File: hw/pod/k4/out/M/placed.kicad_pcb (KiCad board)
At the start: 6 copper layers, 15.5 x 12 mm, 37 parts, among them J10 TestPoint_Pad_D1.0mm, J11 TestPoint_Pad_D1.0mm, J20 CONN-SMD_BM28B0.6-30DS-2-0.35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, J3 TestPoint_Pad_D1.0mm, J4 WirePad_1.0x2.0mm, J5 TestPoint_Pad_D1.0mm, J7 TestPoint_Pad_D1.0mm, J8 TestPoint_Pad_D1.0mm, J9 TestPoint_Pad_D1.0mm, SW1 SW-SMD_4P-L3.0-W2.6-P1.85-LS3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, U2 Knowles_LGA-5_3.5x2.65mm, U3 DSBGA-8_L1.6-W0.9-R2-C4-P0.40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, U4 X2SON-4_L1.0-W1.0-P0.65-TL-EP, U6 SOT-553-5_L1.6-W1.2-P0.50-LS1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

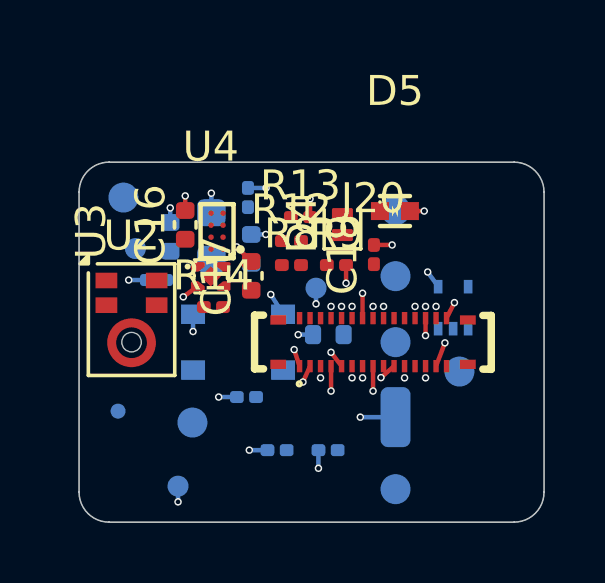
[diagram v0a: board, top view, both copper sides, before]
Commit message: K4 mic-supply filter: R30 33R + C13 on M (MIC_VDDF), k4_noise corrected (P mirror/flip, gap 0.6, JLC 6L stack K4-STACK6): worst-PSRR corner 8.0 dB unfiltered -> 26.4 dB filtered
M re-placed/re-routed (place PASS, 0 unconnected, 0 DRC errors, ERC 0 errors both); P untouched. ECR-0020 rev 5, V9, backlog, vcrm pins, plm 0/0.

Co-Authored-By: Claude Opus 5.5 <noreply@anthropic.com>
Claude-Session: https://claude.ai/code/session_01Wg997D6KFs8bxoAH56jZZJ
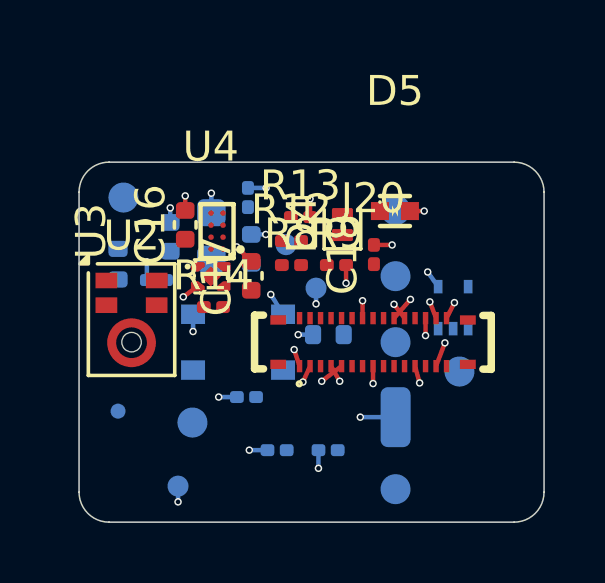
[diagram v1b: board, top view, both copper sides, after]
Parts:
- added R30: R_0402_1005Metric, R_0402_1005Metric, B.Cu at (1.30, 3.40)
- moved TP6 5.02 mm to (6.90, 2.75)
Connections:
- C13 pad 1: MIC_VDD -> MIC_VDDF
- U2 pad 5: MIC_VDD -> MIC_VDDF
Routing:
- net GND: track 16.0 -> 16.9 mm, vias 25 -> 27
- net +3V0: track 4.16 -> 4.74 mm, vias 10 -> 8
- net VBUS_SENSE: vias 1 -> 0
- net USB_DP: vias 1 -> 0
- net USB_DM: vias 1 -> 0
- net TS: vias 1 -> 0
- net MIC_VDD: vias 1 -> 0
- net MIC_DATA: vias 1 -> 0
- net MIC_CLK: vias 1 -> 0
- net I2C_SDA: vias 1 -> 0
- net I2C_SCL: vias 1 -> 0
- net CHG_INT: vias 1 -> 0

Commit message: K4 lid ledge 0.70 (ECR-0022) + C21 0402: M re-routed 0/0, heights from datasheets: lid +0.112 floor +0.163 worst, B2B gap side still fails (C16 -0.10, C17/C9 -0.05)
Noise F02->MIC_VDD worst corner 28.7 dB, k4_checks PASS, plm 0/0. P untouched.

Co-Authored-By: Claude Opus 5.5 <noreply@anthropic.com>
Claude-Session: https://claude.ai/code/session_01Wg997D6KFs8bxoAH56jZZJ
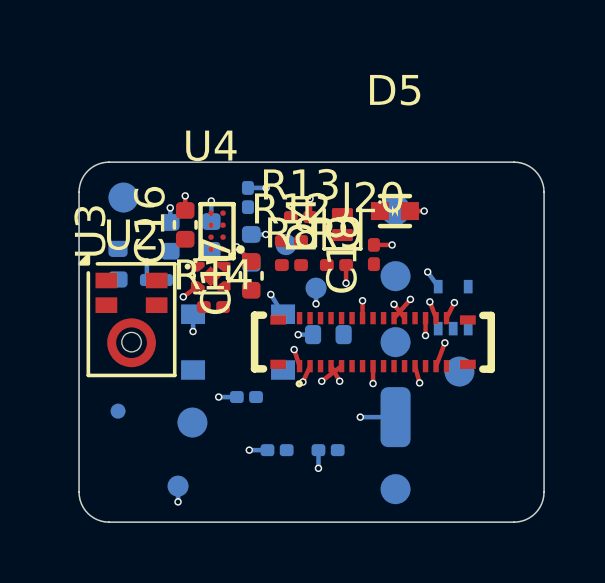
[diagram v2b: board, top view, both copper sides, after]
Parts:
- C21: value C_0603_1608Metric -> C_0402_1005Metric; footprint C_0603_1608Metric -> C_0402_1005Metric

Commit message: K4 guide: BM28 no-key warning, pin-1 dots, photo check, 10-cycle limit
Co-Authored-By: Claude Opus 5.5 <noreply@anthropic.com>
Claude-Session: https://claude.ai/code/session_01Wg997D6KFs8bxoAH56jZZJ
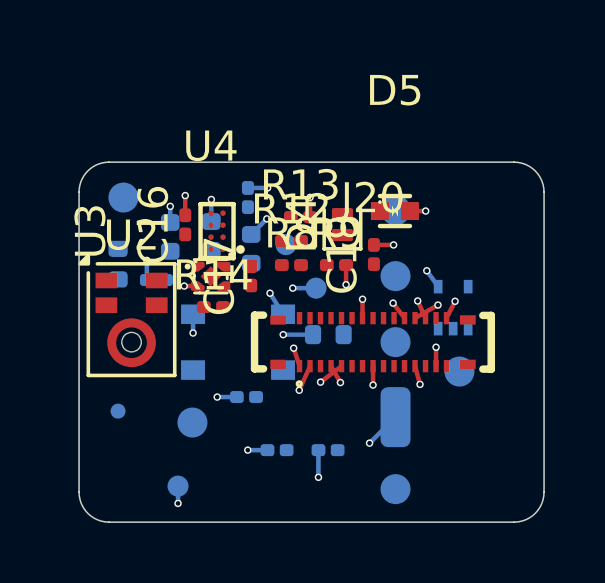
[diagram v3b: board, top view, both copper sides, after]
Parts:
- C16, C17: value C_0402_1005Metric -> C_0201_0603Metric; footprint C_0402_1005Metric -> C_0201_0603Metric
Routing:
- net +3V0: track 4.74 -> 6.29 mm
- net GND: track 17.0 -> 16.8 mm, vias 27 -> 25

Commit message: K4 re-place/route after 9ec84ae: P and M at L 15.5, plain kicad-cli DRC 0 errors / 0 unconnected both; route_net3d GRID env; pin-contract + ECR-0020 + backlog (C9/C17 datasheet check still open)
Co-Authored-By: Claude Opus 5.5 <noreply@anthropic.com>
Claude-Session: https://claude.ai/code/session_01Wg997D6KFs8bxoAH56jZZJ
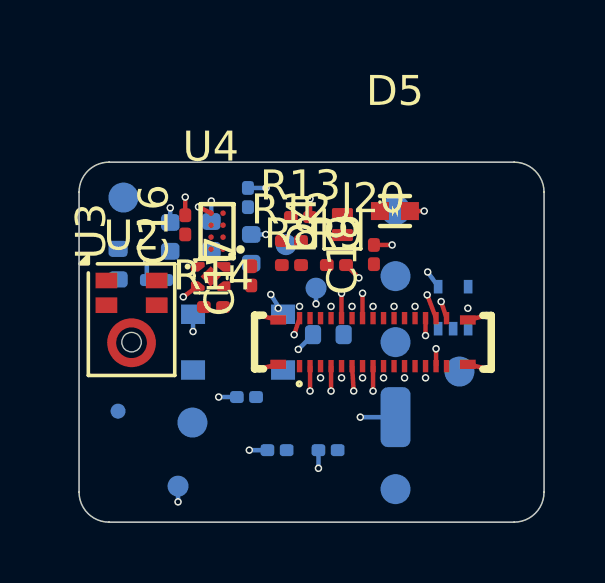
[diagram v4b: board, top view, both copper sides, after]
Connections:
- J20 pad 1: GND -> MIC_VDD
- J20 pad 11: USB_DP -> USB_DM
- J20 pad 13: USB_DM -> USB_DP
- J20 pad 15: GND -> +3V0
- J20 pad 17: +3V0 -> GND
- J20 pad 18: +3V0 -> GND
- J20 pad 19: +3V0 -> LED_K
- J20 pad 21: GND -> MIC_DATA
- J20 pad 22: TS -> GND
- J20 pad 23: I2C_SCL -> CHG_INT
- J20 pad 25: I2C_SDA -> BTN
- J20 pad 26: CHG_INT -> GND
- J20 pad 28: VBAT_SENSE -> GND
- J20 pad 29: BTN -> TS
- J20 pad 30: LED_K -> +3V0
- J20 pad 31: (no net) -> +3V0
- J20 pad 32: (no net) -> +3V0
- J20 pad 33: (no net) -> +3V0
- J20 pad 34: (no net) -> +3V0
- J20 pad 5: GND -> VBAT_SENSE
- J20 pad 6: MIC_VDD -> GND
- J20 pad 7: MIC_DATA -> I2C_SCL
- J20 pad 9: GND -> I2C_SDA
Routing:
- net +3V0: track 6.29 -> 6.92 mm, vias 8 -> 14
- net GND: track 16.8 -> 17.3 mm, vias 25 -> 26
- net VBUS_SENSE: vias 0 -> 1
- net VBAT_SENSE: vias 0 -> 1
- net USB_DP: vias 0 -> 1
- net USB_DM: vias 0 -> 1
- net MIC_DATA: vias 0 -> 1
- net MIC_CLK: vias 0 -> 1
- net LED_K: vias 0 -> 1
- net I2C_SDA: vias 0 -> 1
- net I2C_SCL: vias 0 -> 1
- net CHG_INT: vias 0 -> 1
- net BTN: vias 0 -> 1
